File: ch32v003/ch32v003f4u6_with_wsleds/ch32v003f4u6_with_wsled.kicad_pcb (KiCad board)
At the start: 2 copper layers, 40.6 x 44.5 mm, 30 parts, among them J2 PGM, J4 USB_C_Receptacle_USB2.0, J5 HOLE, J6 HOLE, U1 CH32V003F4U6, U2 3.3vReg

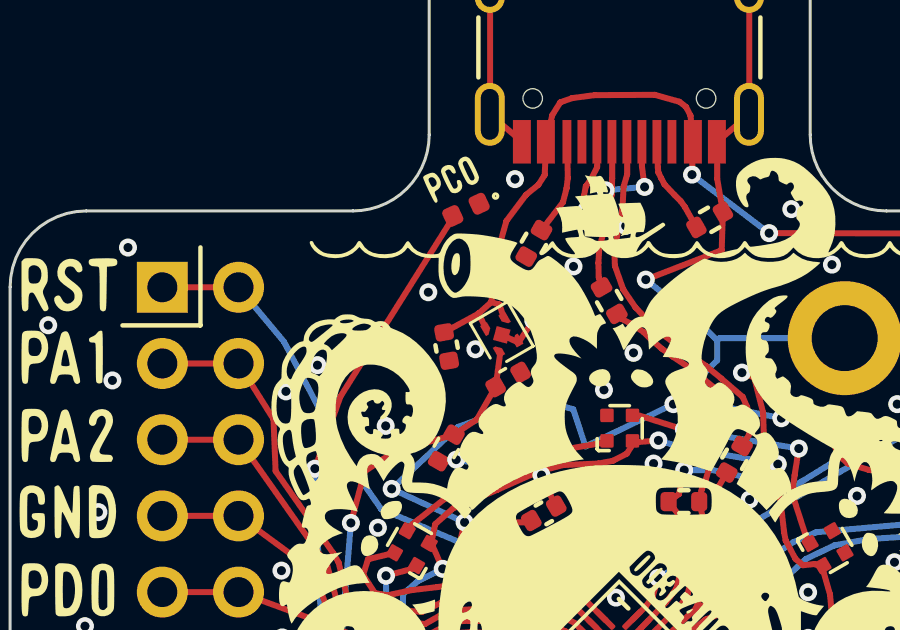
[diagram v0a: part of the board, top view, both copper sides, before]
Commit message: Replace some components with basic parts
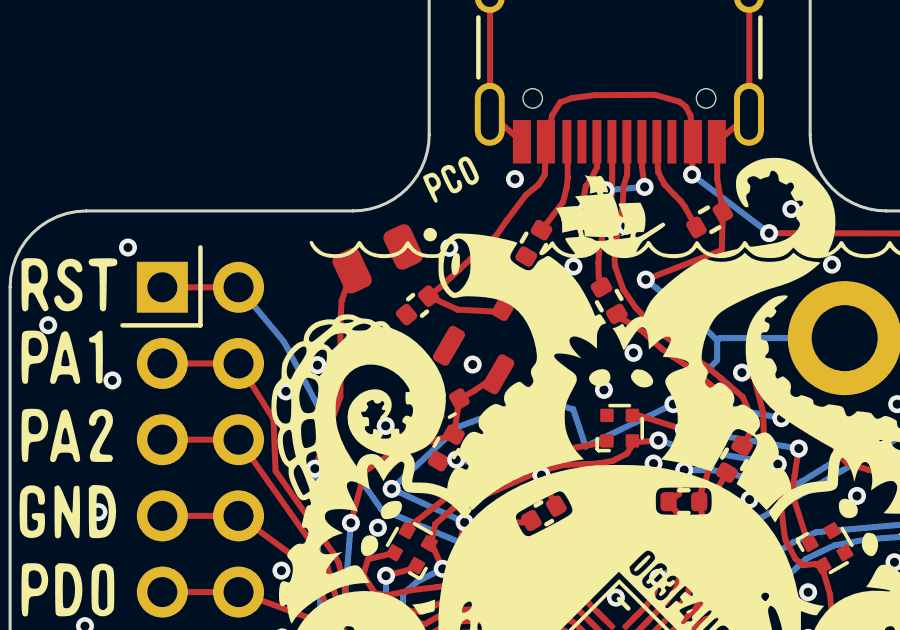
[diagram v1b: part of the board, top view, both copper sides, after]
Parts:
- C1, C2, C3, C4, C5: value 1u -> 4.7u
- D7: footprint LED_SMD:LED_0402_1005Metric -> LED_SMD:LED_0805_2012Metric
- U2: footprint xdfn_reg:xdfn-reg -> Package_TO_SOT_SMD:SOT-23-3
- moved D7 3.37 mm to (91.9, 86.4)
- moved C5 2.23 mm to (94.2, 91.3), turned to -150 degrees
- moved C4 1.68 mm to (93.3, 87.9), turned to -140 degrees
- moved U2 0.40 mm to (95.7, 88.7), turned to 60 degrees
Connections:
- U2 pad 1: VCC -> GND
- U2 pad 2: GND -> VCC
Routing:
- net Net-(D7-A): track 17.6 -> 14.8 mm
- net GND: track 125.3 -> 123.8 mm
- net +5V: track 75.7 -> 76.6 mm
- net VCC: track 41.3 -> 40.7 mm
